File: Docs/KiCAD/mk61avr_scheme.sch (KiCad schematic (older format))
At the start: 43 parts, among them IC1 ATMEGA8-P, K1 CONN_3, P1 CONN_4, SW1 ON/OFF, SW10 2, SW11 X, SW12 RET, SW13 SAVE, SW14 3, SW15 3, SW16 SUB, SW17 LOAD, SW18 4, SW19 XY, SW2 0, SW20 STORE, SW21 5, SW22 ,, SW23 STEP>, SW24 6, SW25 /-/, SW26 LOAD, SW27 7, SW28 POW, SW29 <STEP, SW3 +, SW30 8, SW31 Cx, SW32 K, SW33 9, SW34 Bx, SW35 F, SW36 SW_PUSH, SW4 S/S, SW5 LFT, SW6 1, SW7 -, SW8 GOTO, SW9 RGT

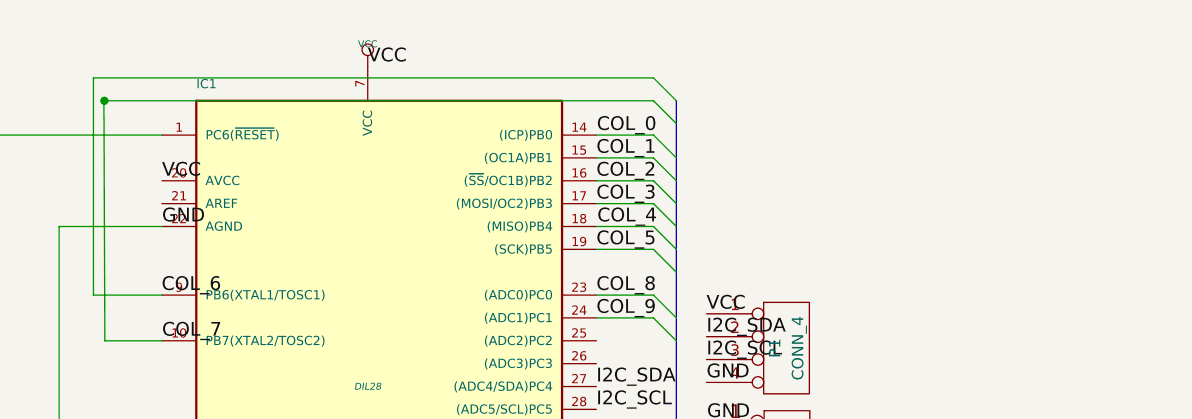
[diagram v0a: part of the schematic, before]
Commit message: USBASP plug added to schematics
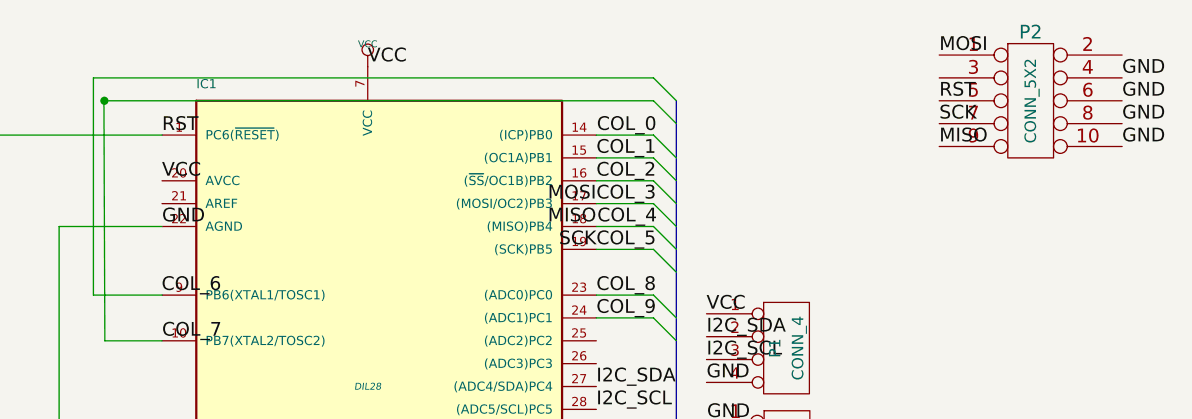
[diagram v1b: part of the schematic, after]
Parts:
- added P2: CONN_5X2, symbol CONN_5X2
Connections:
- net COL_3: now also P2.1
- net COL_4: now also P2.9
- net COL_5: now also P2.7
- net GND: now also P2.10, P2.4, P2.6, P2.8
- net RST: now reaches IC1.1 (PC6(~RESET~)), SW36.2
- net RST: now also P2.5
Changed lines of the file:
@@
 Sheet 1 1
 Title "MK-61-Avr - simulator of programmable calculator MK-61"
-Date "17 jan 2017"
+Date "18 jan 2017"
 Rev "1.0"
 Comp "Private hobby project"
@@
 Text Label 4650 2950 0    60   ~ 0
 GND
+$Comp
+L CONN_5X2 P2
+U 1 1 587F32F4
+P 8450 2400
+F 0 "P2" H 8450 2700 60  0000 C CNN
+F 1 "CONN_5X2" V 8450 2400 50  0000 C CNN
+F 2 "" H 8450 2400 60  0000 C CNN
+F 3 "" H 8450 2400 60  0000 C CNN
+	1    8450 2400
+	1    0    0    -1
+$EndComp
+Text Label 8850 2300 0    60   ~ 0
+GND
+Text Label 8850 2400 0    60   ~ 0
+GND
+Text Label 8850 2500 0    60   ~ 0
+GND
+Text Label 8850 2600 0    60   ~ 0
+GND
+Text Label 8050 2200 0    60   ~ 0
+MOSI
+Text Label 8050 2400 0    60   ~ 0
+RST
+Text Label 8050 2500 0    60   ~ 0
+SCK
+Text Label 8050 2600 0    60   ~ 0
+MISO
+Text Label 4650 2550 0    60   ~ 0
+RST
+Text Label 6550 3050 2    60   ~ 0
+SCK
+Text Label 6550 2950 2    60   ~ 0
+MISO
+Text Label 6550 2850 2    60   ~ 0
+MOSI
 $EndSCHEMATC

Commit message: KiCAD: обновил схему от Алексея
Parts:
- added R1: 10K, symbol R
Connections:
- net COL_3: no longer P2.1
- net COL_4: no longer P2.9
- net COL_5: no longer P2.7
- net GND: now also SW36.2; no longer SW36.1
- net RST: now also SW36.1; no longer SW36.2
- net VCC: no longer IC1.20 (AVCC), IC1.7 (VCC)
- new net MISO: P2.9
- new net MOSI: P2.1
- new net SCK: P2.7
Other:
- moved on the sheet: IC1, SW36

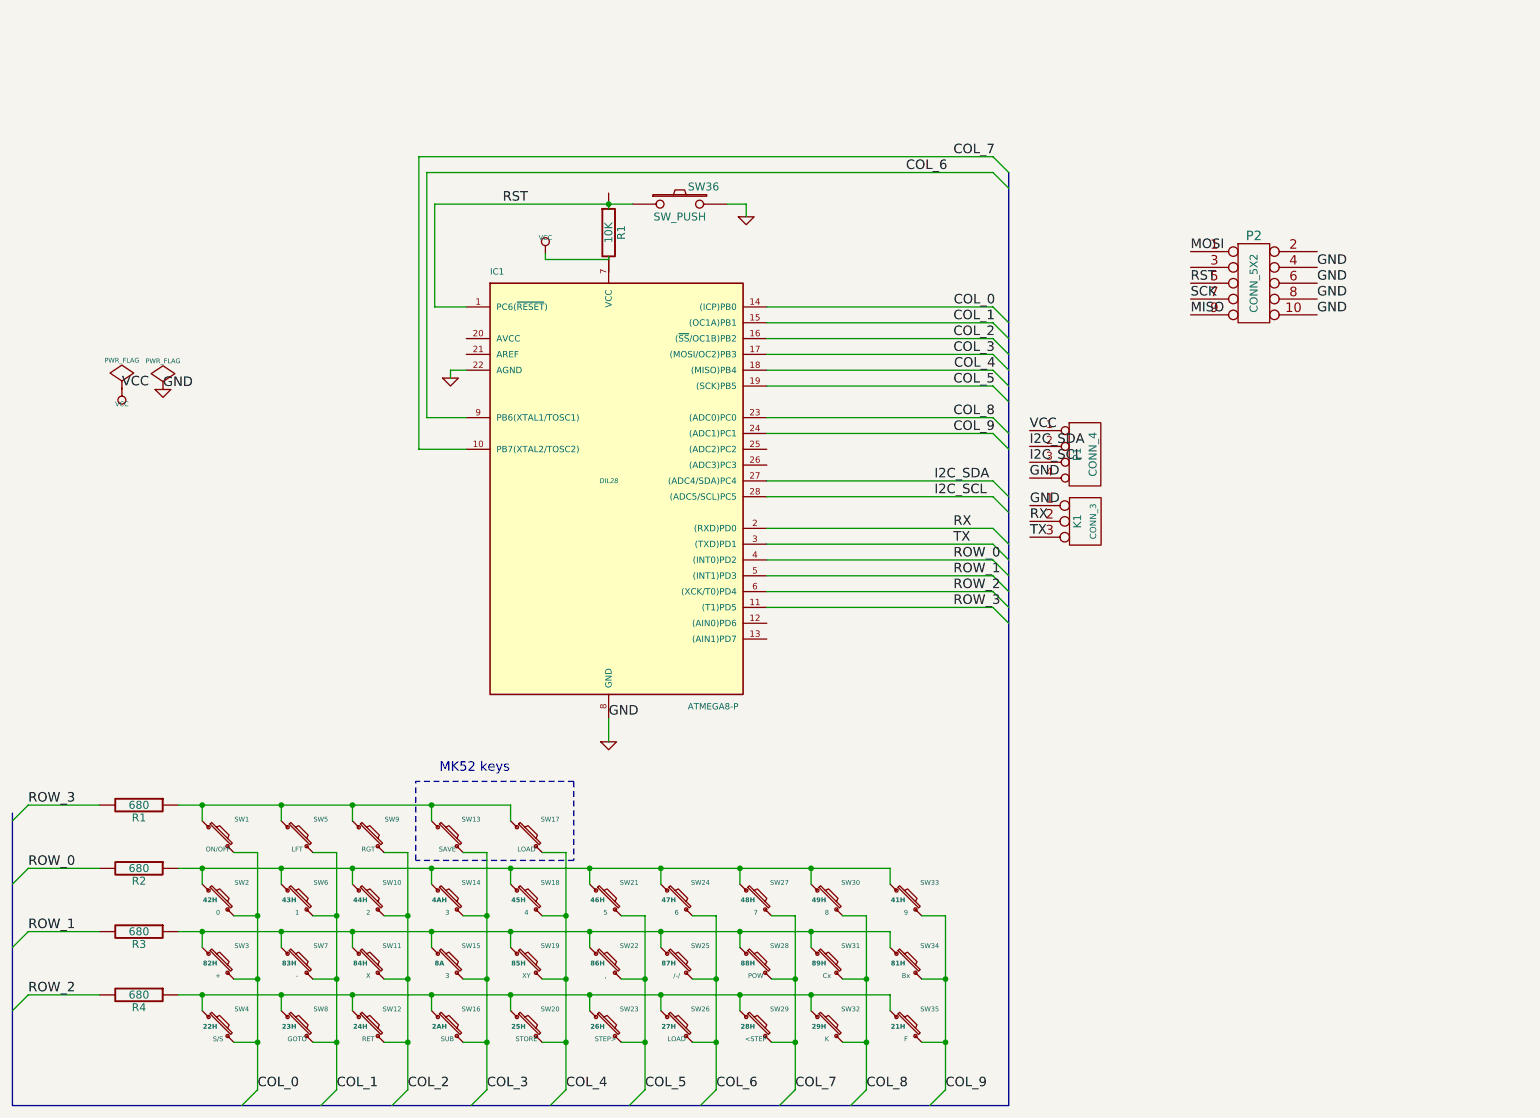
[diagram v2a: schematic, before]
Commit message: KICAD: переделал схему клавиатуры под матрицу 5x8
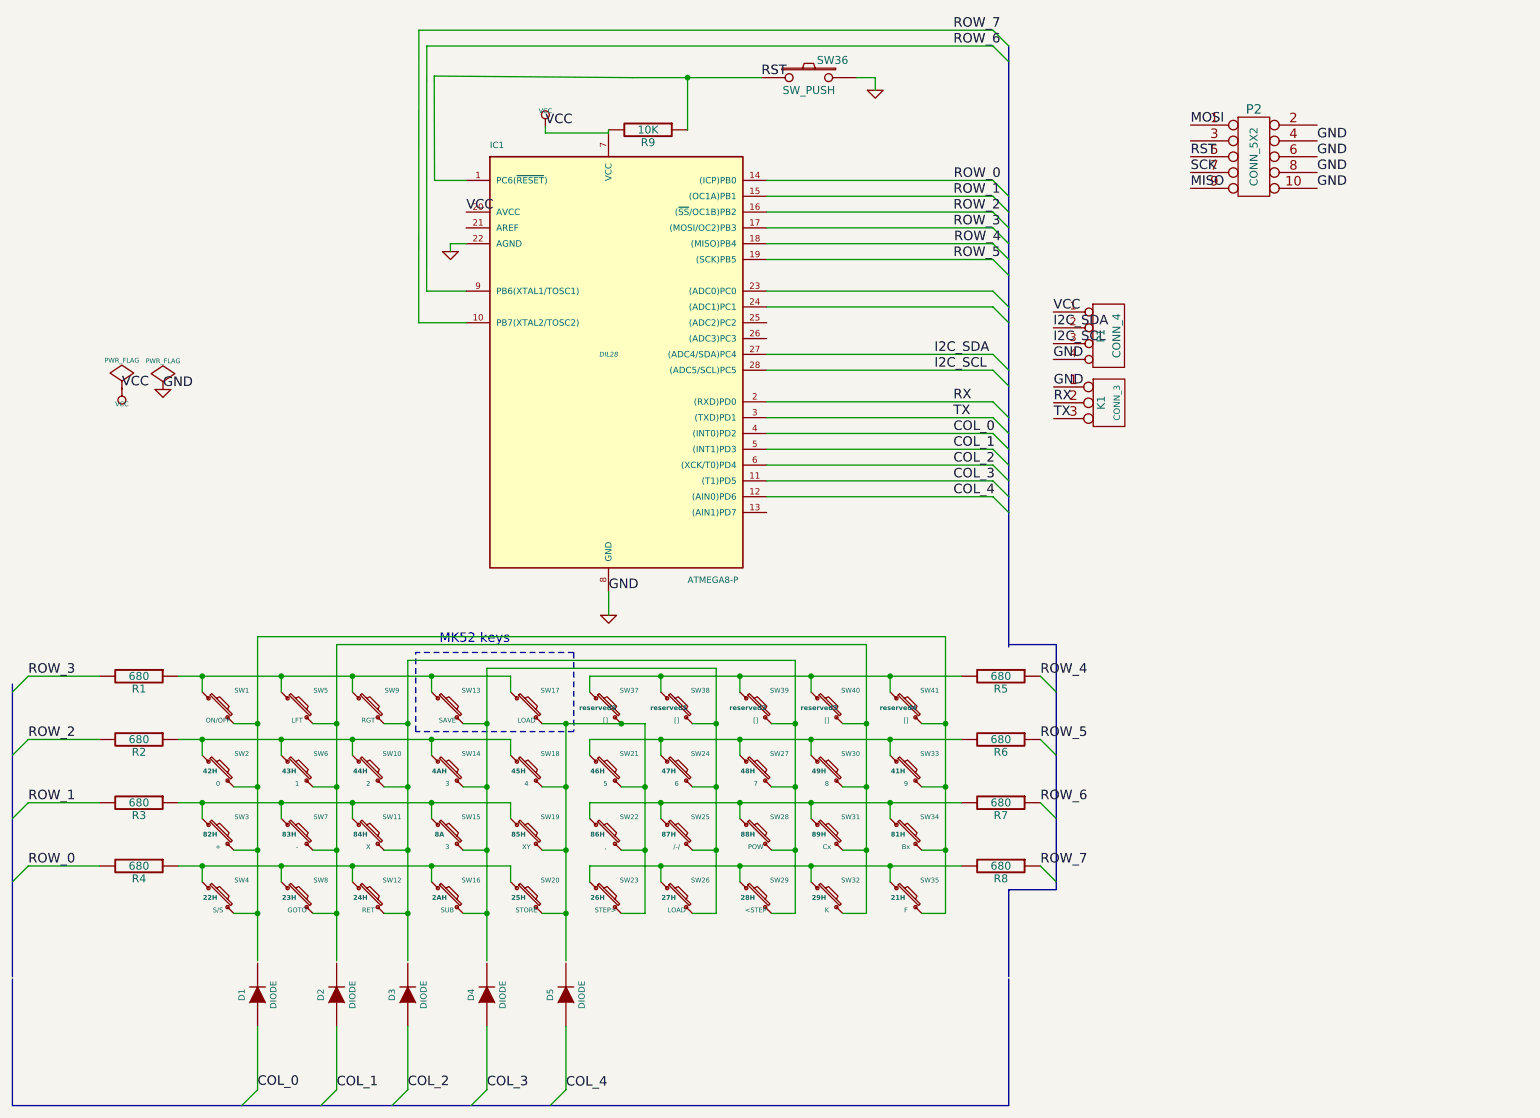
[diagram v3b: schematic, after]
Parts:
- added D1, D2, D3, D4, D5: DIODE, ~, symbol DIODE
- added R5, R6, R7, R8: 680, symbol R
- added SW37, SW38, SW39, SW40, SW41: [], symbol SW_PUSH_SMALL
- renumbered R1 to R9
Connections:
- net labels added: ROW_4, ROW_5, ROW_6, ROW_7
- net labels removed: COL_5, COL_6, COL_7, COL_8, COL_9
- wire segments 122 -> 214
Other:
- moved on the sheet: IC1, K1, P1, P2, R1, R2, R3, R4, R9, SW1, SW10, SW11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

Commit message: схема
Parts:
- R1, R2, R3, R4, R5, R6, R7, R8, R9: symbol R -> R-RESCUE-mk61avr_scheme
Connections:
- wire segments 214 -> 146

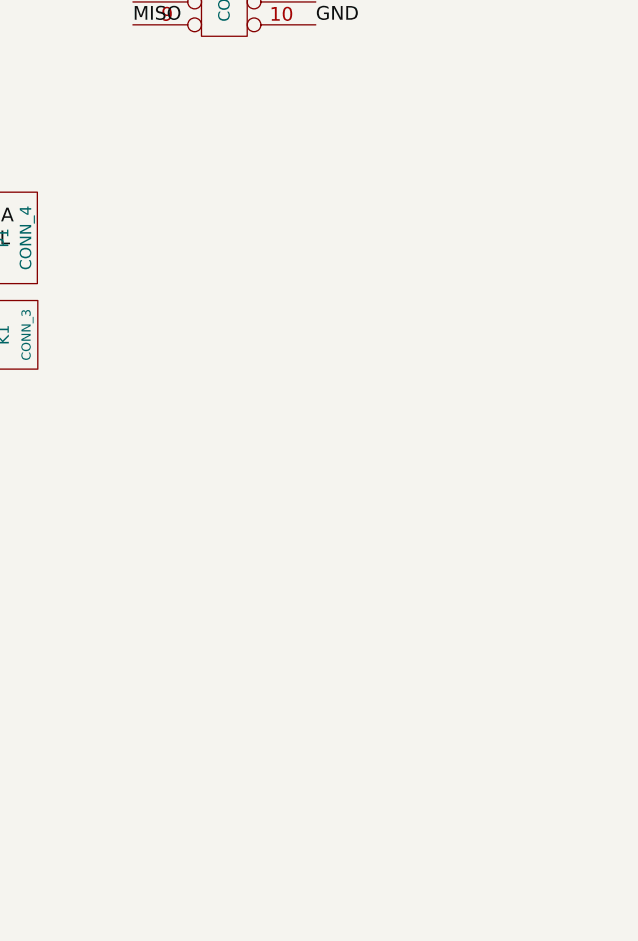
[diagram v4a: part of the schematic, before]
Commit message: KICAD: arduino added
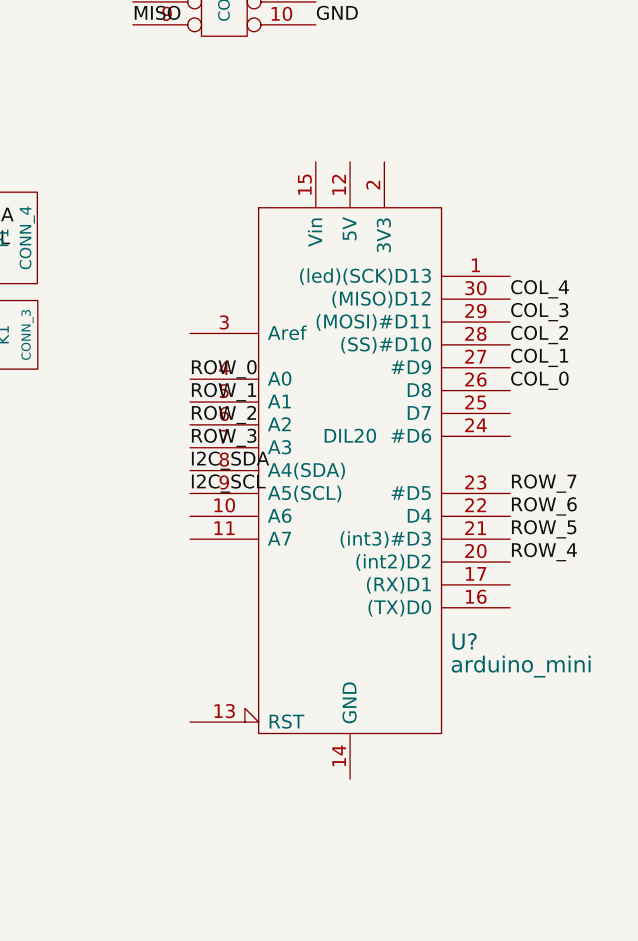
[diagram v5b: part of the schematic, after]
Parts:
- added U?: arduino_mini, DIL20, symbol arduino_mini
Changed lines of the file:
@@
 LIBS:contrib
 LIBS:valves
+LIBS:arduino
 LIBS:mk61avr_scheme-cache
 EELAYER 25 0
@@
 	4869 1430 4869 1100
 Connection ~ 4869 1100
+$Comp
+L arduino_mini U?
+U 1 1 589084D4
+P 9000 3550
+F 0 "U?" H 9500 2600 70  0000 C CNN
+F 1 "arduino_mini" H 9750 2500 70  0000 C CNN
+F 2 "DIL20" H 9000 3500 60  0000 C CNN
+F 3 "" H 9000 3550 60  0001 C CNN
+	1    9000 3550
+	1    0    0    -1
+$EndComp
+Text Label 9700 3000 0    60   ~ 0
+COL_4
+Text Label 9700 3100 0    60   ~ 0
+COL_3
+Text Label 9700 3200 0    60   ~ 0
+COL_2
+Text Label 9700 3300 0    60   ~ 0
+COL_1
+Text Label 9700 3400 0    60   ~ 0
+COL_0
+Text Label 8300 3350 0    60   ~ 0
+ROW_0
+Text Label 8300 3450 0    60   ~ 0
+ROW_1
+Text Label 8300 3550 0    60   ~ 0
+ROW_2
+Text Label 8300 3650 0    60   ~ 0
+ROW_3
+Text Label 9700 4150 0    60   ~ 0
+ROW_4
+Text Label 9700 4050 0    60   ~ 0
+ROW_5
+Text Label 9700 3950 0    60   ~ 0
+ROW_6
+Text Label 9700 3850 0    60   ~ 0
+ROW_7
+Text Label 8300 3750 0    60   ~ 0
+I2C_SDA
+Text Label 8300 3850 0    60   ~ 0
+I2C_SCL
 $EndSCHEMATC
